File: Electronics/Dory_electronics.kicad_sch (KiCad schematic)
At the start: 22 parts, among them J1 Bateria 2S, J10 SHARP_CENTRO_E, J4 Motor B, J5 Motor A, J6 sensor IR, J7 VL53L0X_ESQUERDO, J8 SHARP_CENTRO_D, J9 VL53L0X_DIREITO, U1 LM1117 5V

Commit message: chore: update schematic and PCB
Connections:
- net XSHUT_D: now also DEVKIT1.25 (MISO/19); no longer DEVKIT1.24 (SCK/18)
- net XSHUT_E: now also DEVKIT1.24 (SCK/18); no longer DEVKIT1.25 (MISO/19)
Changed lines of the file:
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@@
+	)
+	(no_connect
+		(at 71.12 67.31)
 	)
 	(no_connect
@@
 	)
 	(no_connect
+		(at 43.18 67.31)
+	)
+	(no_connect
 		(at 162.052 108.2548)
 	)
@@
 	(no_connect
 		(at 162.0012 102.6922)
-	)
-	(no_connect
-		(at 43.18 67.31)
-	)
-	(no_connect
-		(at 71.12 67.31)
 	)
 	(no_connect
@@
 		)
 	)
+	(global_label "XSHUT_E"
+		(shape output)
+		(at 162.179 94.996 0)
+		(effects
+			(font
+				(size 1.27 1.27)
+			)
+			(justify left)
+		)
+		(property "Intersheetrefs" "${INTERSHEET_REFS}"
+			(at 162.179 94.996 0)
+			(effects
+				(font
+					(size 1.27 1.27)
+				)
+				(hide yes)
+			)
+		)
+	)
+	(global_label "BIN1"
+		(shape output)
+		(at 125.857 94.996 180)
+		(effects
+			(font
+				(size 1.27 1.27)
+			)
+			(justify right)
+		)
+		(property "Intersheetrefs" "${INTERSHEET_REFS}"
+			(at 125.857 94.996 0)
+			(effects
+				(font
+					(size 1.27 1.27)
+				)
+				(hide yes)
+			)
+		)
+	)
+	(global_label "BO2"
+		(shape input)
+		(at 66.167 32.766 90)
+		(fields_autoplaced yes)
+		(effects
+			(font
+				(size 1.016 1.016)
+			)
+			(justify left)
+		)
+		(property "Intersheetrefs" "${INTERSHEET_REFS}"
+			(at 66.167 27.3301 90)
+			(effects
+				(font
+					(size 1.27 1.27)
+				)
+				(justify left)
+				(hide yes)
+			)
+		)
+	)
+	(global_label "2S"
+		(shape input)
+		(at 55.88 147.32 90)
+		(fields_autoplaced yes)
+		(effects
+			(font
+				(size 1.27 1.27)
+			)
+			(justify left)
+		)
+		(property "Intersheetrefs" "${INTERSHEET_REFS}"
+			(at 55.88 141.9158 90)
+			(effects
+				(font
+					(size 1.27 1.27)
+				)
+				(justify left)
+				(hide yes)
+			)
+		)
+	)
+	(global_label "SCL"
+		(shape input)
+		(at 237.49 71.12 180)
+		(effects
+			(font
+				(size 1.27 1.27)
+			)
+			(justify right)
+		)
+		(property "Intersheetrefs" "${INTERSHEET_REFS}"
+			(at 237.49 71.12 0)
+			(effects
+				(font
+					(size 1.27 1.27)
+				)
+				(hide yes)
+			)
+		)
+	)
 	(global_label "XSHUT_D"
 		(shape output)
-		(at 162.179 94.996 0)
-		(effects
-			(font
-				(size 1.27 1.27)
-			)
-			(justify left)
-		)
-		(property "Intersheetrefs" "${INTERSHEET_REFS}"
-			(at 162.179 94.996 0)
-			(effects
-				(font
-					(size 1.27 1.27)
-				)
-				(hide yes)
-			)
-		)
-	)
-	(global_label "BIN1"
-		(shape output)
-		(at 125.857 94.996 180)
-		(effects
-			(font
-				(size 1.27 1.27)
-			)
-			(justify right)
-		)
-		(property "Intersheetrefs" "${INTERSHEET_REFS}"
-			(at 125.857 94.996 0)
-			(effects
-				(font
-					(size 1.27 1.27)
-				)
-				(hide yes)
-			)
-		)
-	)
-	(global_label "BO2"
-		(shape input)
-		(at 66.167 32.766 90)
-		(fields_autoplaced yes)
-		(effects
-			(font
-				(size 1.016 1.016)
-			)
-			(justify left)
-		)
-		(property "Intersheetrefs" "${INTERSHEET_REFS}"
-			(at 66.167 27.3301 90)
-			(effects
-				(font
-					(size 1.27 1.27)
-				)
-				(justify left)
-				(hide yes)
-			)
-		)
-	)
-	(global_label "2S"
-		(shape input)
-		(at 55.88 147.32 90)
-		(fields_autoplaced yes)
-		(effects
-			(font
-				(size 1.27 1.27)
-			)
-			(justify left)
-		)
-		(property "Intersheetrefs" "${INTERSHEET_REFS}"
-			(at 55.88 141.9158 90)
-			(effects
-				(font
-					(size 1.27 1.27)
-				)
-				(justify left)
-				(hide yes)
-			)
-		)
-	)
-	(global_label "SCL"
-		(shape input)
-		(at 237.49 71.12 180)
-		(effects
-			(font
-				(size 1.27 1.27)
-			)
-			(justify right)
-		)
-		(property "Intersheetrefs" "${INTERSHEET_REFS}"
-			(at 237.49 71.12 0)
-			(effects
-				(font
-					(size 1.27 1.27)
-				)
-				(hide yes)
-			)
-		)
-	)
-	(global_label "XSHUT_E"
-		(shape output)
 		(at 162.179 92.4306 0)

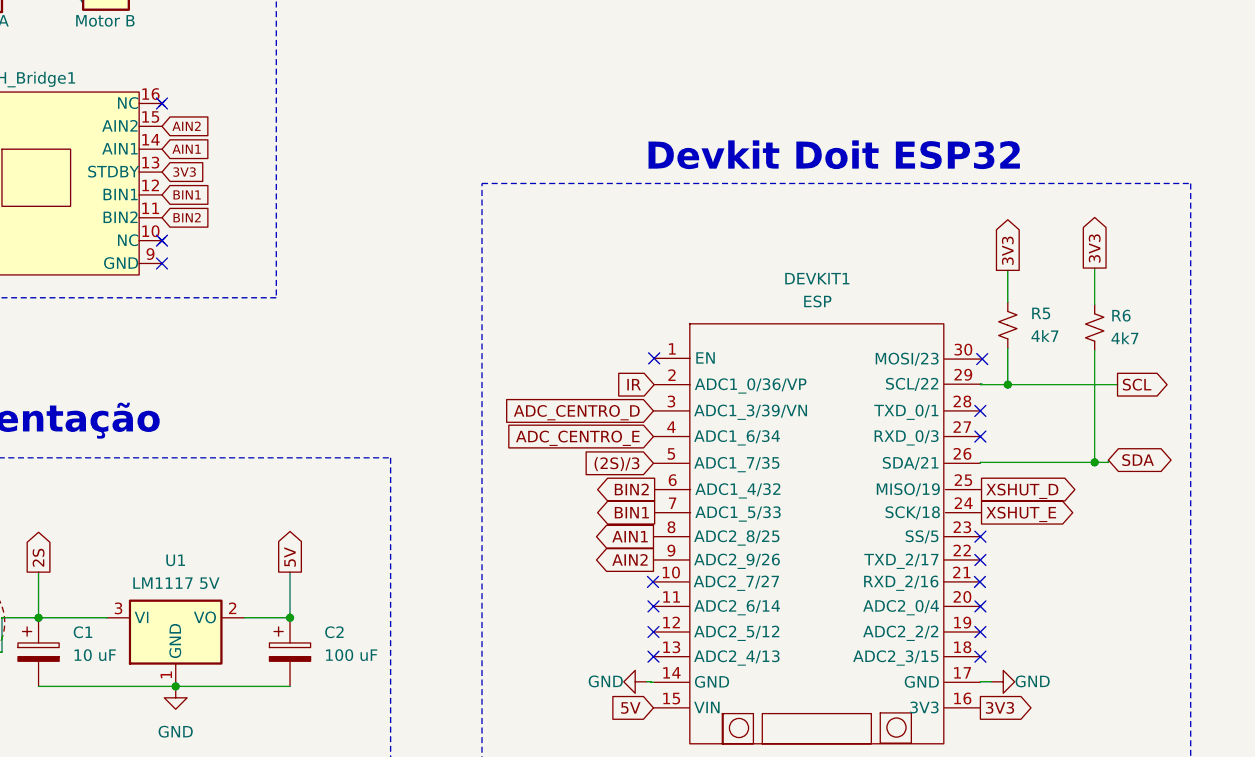
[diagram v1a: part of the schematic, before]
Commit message: chore: redo paths to homemade pcb
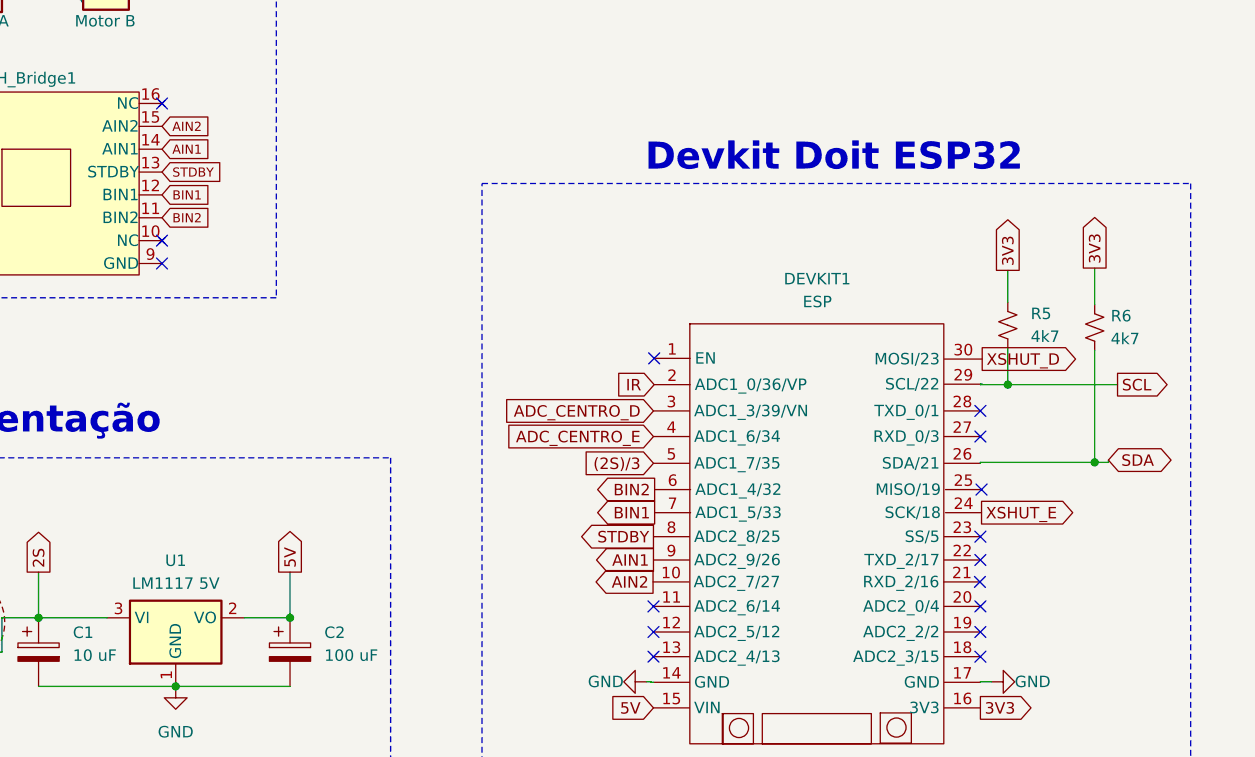
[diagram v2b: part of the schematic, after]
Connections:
- net 3V3: no longer H_Bridge1.13 (STDBY)
- net AIN1: now also DEVKIT1.9 (ADC2_9/26); no longer DEVKIT1.8 (ADC2_8/25)
- net AIN2: now also DEVKIT1.10 (ADC2_7/27); no longer DEVKIT1.9 (ADC2_9/26)
- net XSHUT_D: now also DEVKIT1.30 (MOSI/23); no longer DEVKIT1.25 (MISO/19)
- new net STDBY: DEVKIT1.8 (ADC2_8/25), H_Bridge1.13 (STDBY)
- no-connect marks 19 -> 18

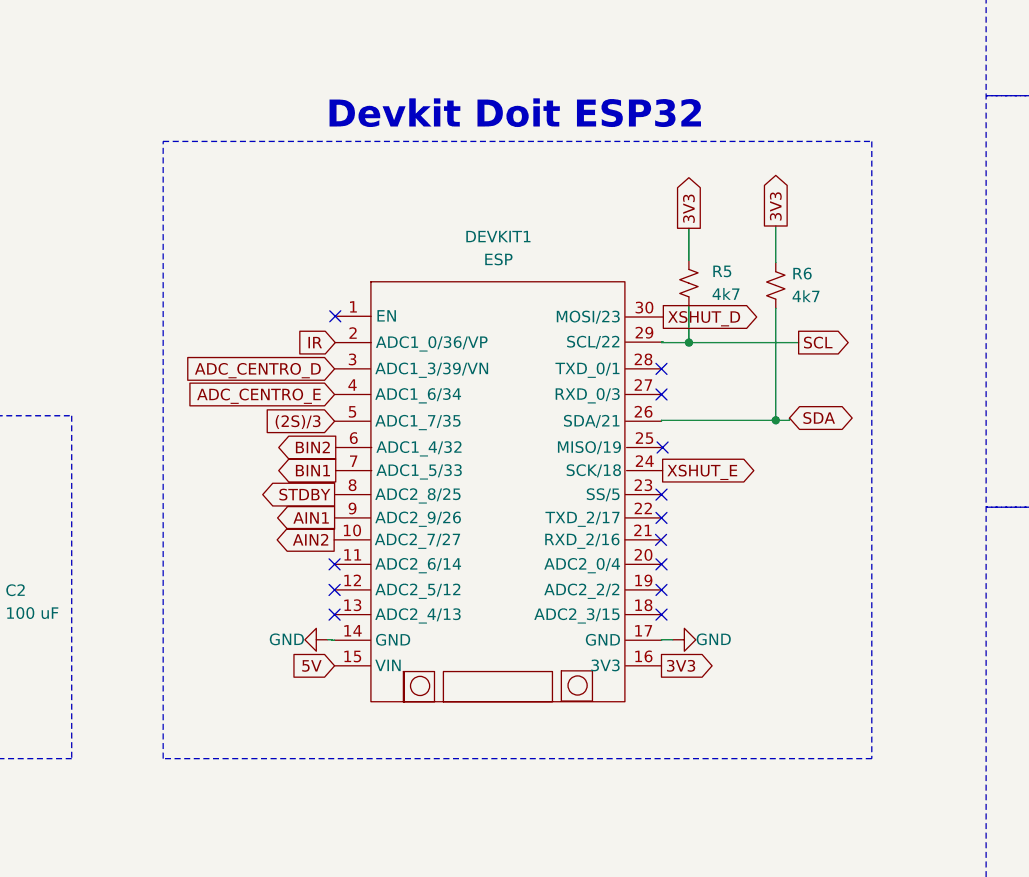
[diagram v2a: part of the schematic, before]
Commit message: chore: update esp32 lib sym and footprint
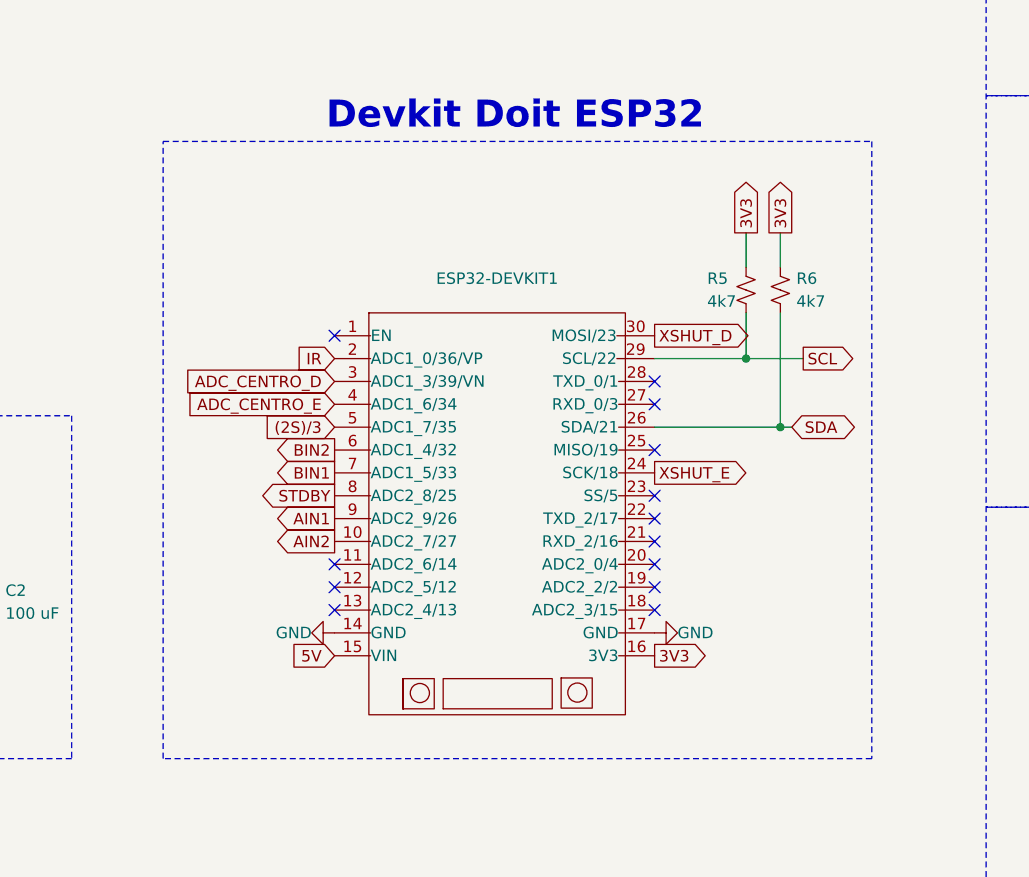
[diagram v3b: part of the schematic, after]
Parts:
- removed DEVKIT1: ESP, esp32_devkit_v1_doit:esp32_devkit_v1_doit, symbol esp32_devkit_v1_doit:ESP
- added ESP32-DEVKIT1: ~, esp32_devkit_v1_doit:esp32_devkit_v1_doit, symbol esp32_devkit_v1_doit:ESP32-DEVKIT
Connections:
- net (2S)/3: now also ESP32-DEVKIT1.5 (ADC1_7/35)
- net 3V3: now also ESP32-DEVKIT1.16 (3V3)
- net 5V: now also ESP32-DEVKIT1.15 (VIN)
- net ADC_CENTRO_D: now also ESP32-DEVKIT1.3 (ADC1_3/39/VN)
- net ADC_CENTRO_E: now also ESP32-DEVKIT1.4 (ADC1_6/34)
- net AIN1: now also ESP32-DEVKIT1.9 (ADC2_9/26)
- net AIN2: now also ESP32-DEVKIT1.10 (ADC2_7/27)
- net BIN1: now also ESP32-DEVKIT1.7 (ADC1_5/33)
- net BIN2: now also ESP32-DEVKIT1.6 (ADC1_4/32)
- net GND: now also ESP32-DEVKIT1.14 (GND), ESP32-DEVKIT1.17 (GND)
- net IR: now also ESP32-DEVKIT1.2 (ADC1_0/36/VP)
- net SCL: now also ESP32-DEVKIT1.29 (SCL/22)
- net SDA: now also ESP32-DEVKIT1.26 (SDA/21)
- net STDBY: now also ESP32-DEVKIT1.8 (ADC2_8/25)
- net XSHUT_D: now also ESP32-DEVKIT1.30 (MOSI/23)
- net XSHUT_E: now also ESP32-DEVKIT1.24 (SCK/18)

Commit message: chore: Add/Update 3D models on PCB
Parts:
- 6_Pins_Button1: footprint Button_Switch_THT:Nidec_Copal_SH-7010C -> esp32_devkit_v1_doit:Push_Button_6_pins
- ESP32-DEVKIT1: footprint esp32_devkit_v1_doit:esp32_devkit_v1_doit -> esp32_devkit_v1_doit:esp32_with_headers
- H_Bridge1: footprint esp32_devkit_v1_doit:H_Bridge -> esp32_devkit_v1_doit:H_Bridge_with_headers
- J4, J5: footprint Connector_JST:JST_XH_B2B-XH-AM_1x02_P2.50mm_Vertical -> Connector_JST:JST_XH_B2B-XH-A_1x02_P2.50mm_Vertical
- J7, J9: footprint Connector_JST:JST_XH_B5B-XH-AM_1x05_P2.50mm_Vertical -> Connector_JST:JST_XH_B5B-XH-A_1x05_P2.50mm_Vertical
- U1: footprint Package_TO_SOT_THT:TO-220-3_Horizontal_TabDown -> Package_TO_SOT_THT:TO-220-3_Vertical
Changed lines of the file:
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@@
 			)
 		)
-		(property "Footprint" "Button_Switch_THT:Nidec_Copal_SH-7010C"
+		(property "Footprint" "esp32_devkit_v1_doit:Push_Button_6_pins"
 			(at 44.45 106.68 0)
 			(effects
@@
 			)
 		)
-		(property "Footprint" "Connector_JST:JST_XH_B5B-XH-AM_1x05_P2.50mm_Vertical"
+		(property "Footprint" "Connector_JST:JST_XH_B5B-XH-A_1x05_P2.50mm_Vertical"
 			(at 242.57 71.12 0)
 			(effects
@@
 			)
 		)
-		(property "Footprint" "esp32_devkit_v1_doit:esp32_devkit_v1_doit"
+		(property "Footprint" "esp32_devkit_v1_doit:esp32_with_headers"
 			(at 143.51 88.9 0)
 			(effects
@@
 			)
 		)
-		(property "Footprint" "esp32_devkit_v1_doit:H_Bridge"
+		(property "Footprint" "esp32_devkit_v1_doit:H_Bridge_with_headers"
 			(at 56.9468 55.6768 0)
 			(effects
@@
 			)
 		)
-		(property "Footprint" "Connector_JST:JST_XH_B5B-XH-AM_1x05_P2.50mm_Vertical"
+		(property "Footprint" "Connector_JST:JST_XH_B5B-XH-A_1x05_P2.50mm_Vertical"
 			(at 242.57 88.9 0)
 			(effects
@@
 			)
 		)
-		(property "Footprint" "Connector_JST:JST_XH_B2B-XH-AM_1x02_P2.50mm_Vertical"
+		(property "Footprint" "Connector_JST:JST_XH_B2B-XH-A_1x02_P2.50mm_Vertical"
 			(at 63.627 37.846 0)
 			(effects
@@
 			)
 		)
-		(property "Footprint" "Package_TO_SOT_THT:TO-220-3_Horizontal_TabDown"
+		(property "Footprint" "Package_TO_SOT_THT:TO-220-3_Vertical"
 			(at 72.644 106.68 0)
 			(effects
@@
 			)
 		)
-		(property "Footprint" "Connector_JST:JST_XH_B2B-XH-AM_1x02_P2.50mm_Vertical"
+		(property "Footprint" "Connector_JST:JST_XH_B2B-XH-A_1x02_P2.50mm_Vertical"
 			(at 49.53 38.1 0)
 			(effects

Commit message: chore: update PCB and create BOM file
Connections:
- net SCL: now also J7.4 (Pin_4), J9.4 (Pin_4); no longer J7.3 (Pin_3), J9.3 (Pin_3)
- net SDA: now also J7.3 (Pin_3), J9.3 (Pin_3); no longer J7.4 (Pin_4), J9.4 (Pin_4)
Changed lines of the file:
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@@
 	(global_label "SDA"
 		(shape bidirectional)
-		(at 237.49 91.44 180)
-		(effects
-			(font
-				(size 1.27 1.27)
-			)
-			(justify right)
-		)
-		(property "Intersheetrefs" "${INTERSHEET_REFS}"
-			(at 237.49 91.44 0)
+		(at 237.49 88.9 180)
+		(effects
+			(font
+				(size 1.27 1.27)
+			)
+			(justify right)
+		)
+		(property "Intersheetrefs" "${INTERSHEET_REFS}"
+			(at 237.49 88.9 0)
 			(effects
 				(font
@@
 	(global_label "SDA"
 		(shape bidirectional)
-		(at 237.49 73.66 180)
-		(effects
-			(font
-				(size 1.27 1.27)
-			)
-			(justify right)
-		)
-		(property "Intersheetrefs" "${INTERSHEET_REFS}"
-			(at 237.49 73.66 0)
+		(at 237.49 71.12 180)
+		(effects
+			(font
+				(size 1.27 1.27)
+			)
+			(justify right)
+		)
+		(property "Intersheetrefs" "${INTERSHEET_REFS}"
+			(at 237.49 71.12 0)
 			(effects
 				(font
@@
 	(global_label "SCL"
 		(shape input)
-		(at 237.49 88.9 180)
-		(effects
-			(font
-				(size 1.27 1.27)
-			)
-			(justify right)
-		)
-		(property "Intersheetrefs" "${INTERSHEET_REFS}"
-			(at 237.49 88.9 0)
+		(at 237.49 91.44 180)
+		(effects
+			(font
+				(size 1.27 1.27)
+			)
+			(justify right)
+		)
+		(property "Intersheetrefs" "${INTERSHEET_REFS}"
+			(at 237.49 91.44 0)
 			(effects
 				(font
@@
 	(global_label "SCL"
 		(shape input)
-		(at 237.49 71.12 180)
-		(effects
-			(font
-				(size 1.27 1.27)
-			)
-			(justify right)
-		)
-		(property "Intersheetrefs" "${INTERSHEET_REFS}"
-			(at 237.49 71.12 0)
-			(effects
-				(font
+		(at 237.49 73.66 180)
+		(effects
+			(font
+				(size 1.27 1.27)
+			)
+			(justify right)
+		)
+		(property "Intersheetrefs" "${INTERSHEET_REFS}"
+			(at 237.49 73.66 0)
+			(effects
+				(font
